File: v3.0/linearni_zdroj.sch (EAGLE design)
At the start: 29 parts, among them IC1 LM358N, IC2 LM358N, Q1 TIP120, Q2 TIP120

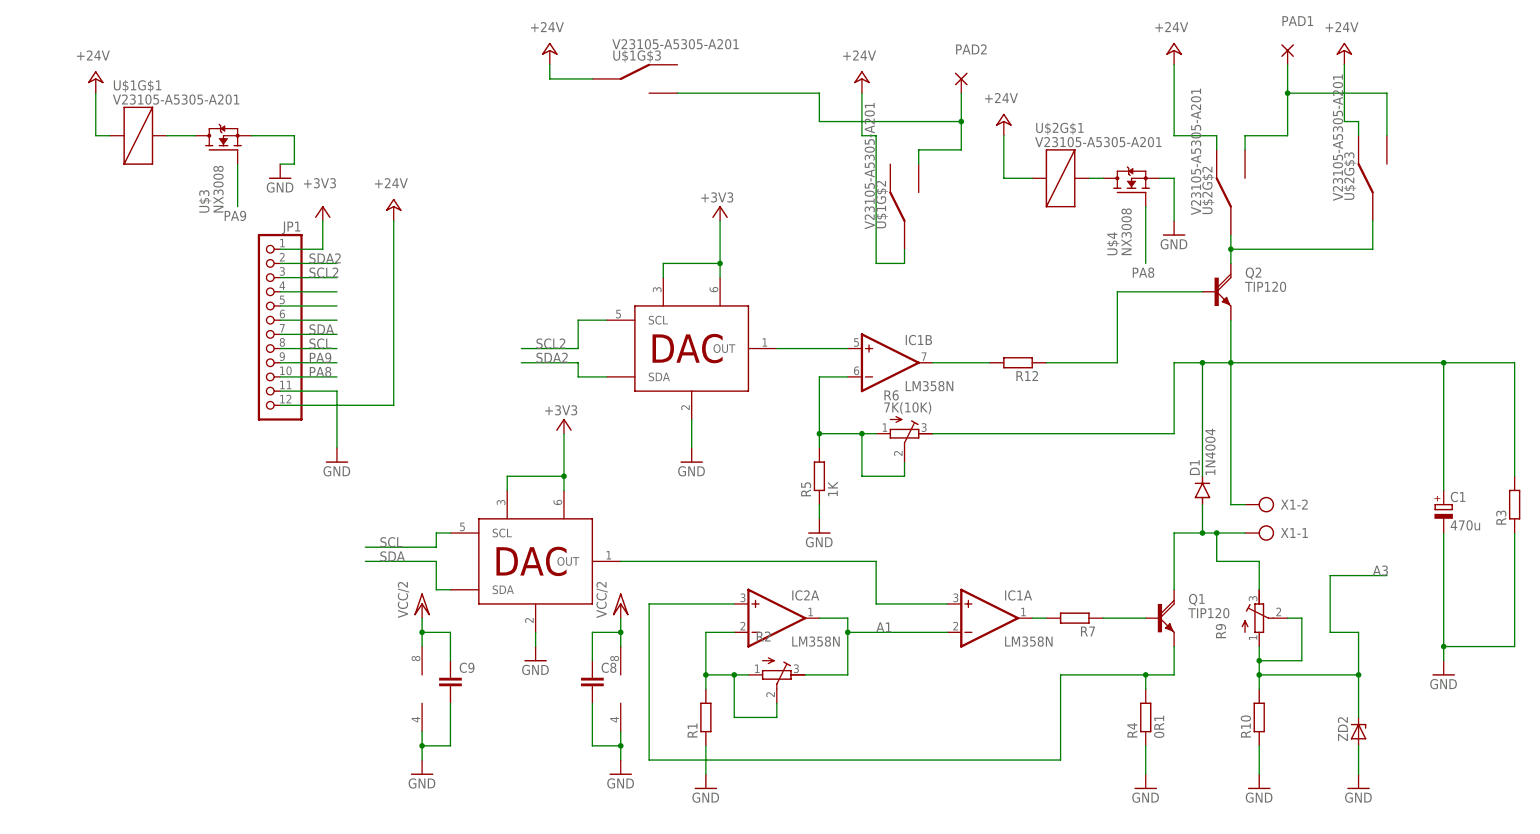
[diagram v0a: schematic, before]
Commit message: zpřehlednění schématu
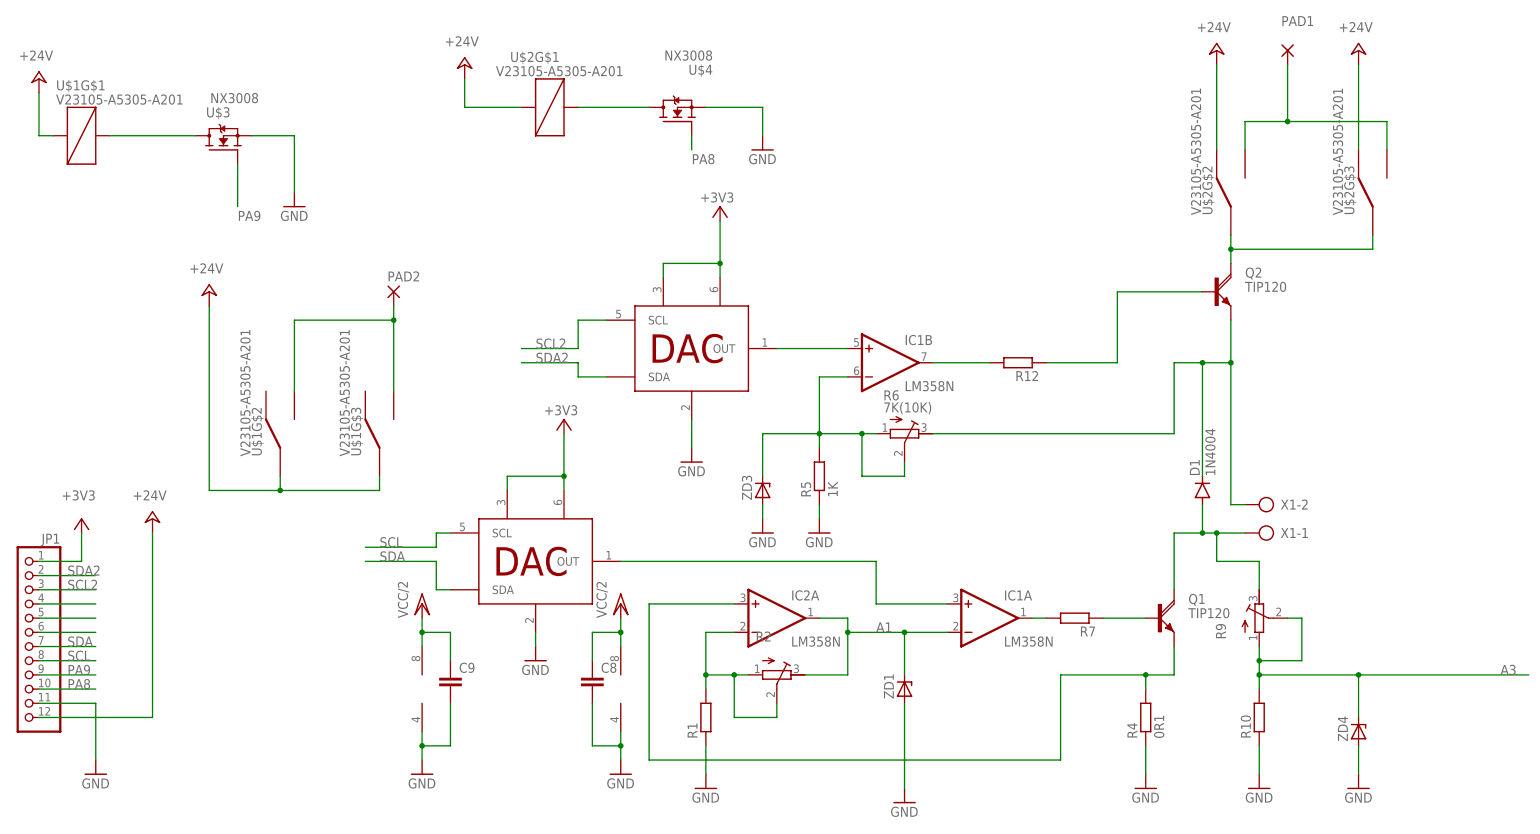
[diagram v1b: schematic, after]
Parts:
- removed C1: 470u, rcl:CPOL-EUE3.5-8
- removed R3: (no value), rcl:R-EU_R0805
- removed ZD2: (no value), devices:DIODE_ZENER5
- added ZD1, ZD3, ZD4: (no value), devices:DIODE_ZENER"2
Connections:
- net A1: now also ZD1.C
- net A3: now also ZD4.C; no longer ZD2.C
- net GND: now also ZD1.A, ZD3.A, ZD4.A; no longer C1.-, R3.1, ZD2.A
- net N$11: now also ZD3.C
- net N$13: no longer C1.+, R3.2
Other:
- moved on the sheet: JP1, PAD2, U$1G$1, U$1G$2, U$1G$3, U$2G$1, U$2G$3, U$4

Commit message: přidány pull-up rezistory I2C
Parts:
- added PAD3, PAD4: (no value), wirepad:3,81/1,4
- added R11, R13, R3, R8: (no value), rcl_my:R-EU_M0805
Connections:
- net +24V: now also PAD3.P, U$2G$2.3, U$2G$3.3; no longer U$2G$2.2, U$2G$3.2
- net +3V3: now also R11.2, R13.2, R3.2, R8.2
- net GND: now also PAD4.P
- net N$10: now also U$2G$2.2, U$2G$3.2; no longer U$2G$2.3, U$2G$3.3
- net SCL: now also R13.1
- net SCL2: now also R8.1
- net SDA: now also R3.1
- net SDA2: now also R11.1
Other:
- moved on the sheet: C9, PAD2, U$1G$2, U$1G$3

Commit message: deska lineárního regulátoru
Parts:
- removed C8: (no value), rcl:C-EUC0805
- added C1: (no value), rcl:C-EUC0805
- added R14: (no value), rcl:R-EU_R0805
- added ZD2: (no value), devices:DIODE_ZENER7
- D1: value 1N4004 -> (none); device diode:1N4004 -> devices:DIODE7
- Q1: value TIP120 -> IRFZ34NAV; device transistor-power:TIP120 -> devices:IRFZ34NAV
- R2, R6, R9: device rcl:R-TRIMM3339P -> pot:TRIM_EU-CA6V
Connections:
- removed net A1: IC1A.-IN, IC2A.OUT, R2.E, ZD1.C
- removed net A3: R10.2, R9.A, R9.S, ZD4.C
- removed net N$11: IC1B.-IN, R5.2, R6.A, R6.S, ZD3.C
- removed net N$14: JP1.4
- removed net N$15: JP1.5
- removed net N$18: JP1.6
- removed net VCC/2: C8.1, C9.1, IC1P.V+, IC2P.V+
- new net ADC0: IC2A.OUT, IC2B.-IN, JP1.6, R2.E, ZD1.C
- new net ADC1: JP1.5, R10.2, R9.A, R9.S, ZD4.C
- new net ADC2: IC1B.-IN, JP1.4, R5.2, R6.A, R6.S, ZD3.C
- new net N$20: C1.1, IC2A.+IN, R14.1
- net +24V: now also IC1P.V+, R7.2
- net GND: now also C1.2, ZD2.A; no longer C8.2
- net N$1: now also Q1.S, R14.2; no longer IC2A.+IN, Q1.E
- net N$2: now also IC2B.OUT, Q1.G; no longer IC1A.OUT, R7.2
- net N$5: now also C9.1, IC2P.V+, ZD2.C; no longer Q1.B
- net N$6: now also IC2B.+IN; no longer IC1A.+IN
- net N$7: now also Q1.D; no longer Q1.C
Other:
- moved on the sheet: R7

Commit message: přidání 3D modelu úpravy dokumentace
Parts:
- R1, R11, R13, R3, R8: device rcl_my:R-EU_M0805 -> rcl:R-EU_R0805

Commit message: upratování schémy, dokumentace lineárního regulátoru napětí
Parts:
- removed PAD1, PAD2: (no value), wirepad:3,81/1,4
- added C2: 10n, rcl:C-EUC0805
- added VSTUP-BUCK, VÝSTUP-BUCK: (no value), wirepad:3,81/1,4
- R11, R8: value (none) -> 5K
- R12: value (none) -> 360R
- renumbered PAD3 to 24V
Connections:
- net N$13 renamed +
- net N$8 renamed NAPAJENI-REG
- net +24V: now also C2.1
- net GND: now also C2.2
- net N$10: now also VÝSTUP-BUCK.P; no longer PAD1.P
- net N$19: now also VSTUP-BUCK.P; no longer PAD2.P
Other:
- note added: "Lineární regulátor napětí"
- note added: "Relé napájení pulzního regulátoru"
- note added: "Relé zdroje lineárních regulátorů"
- note added: "napájení OZ"
- moved on the sheet: IC1B, Q2, R11, R12, R13, R3, R5, R6, R8, U$1G$2, U$1G$3, U$2G$1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

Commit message: zase sem se jednou ve škole něco naučil
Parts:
- removed C1: (no value), rcl:C-EUC0805
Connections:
- removed net N$1: Q1.S, R14.2, R4.2
- net GND: now also R14.1; no longer C1.2
- net N$2: now also R14.2
- net N$20: now also Q1.S, R4.2; no longer C1.1, R14.1
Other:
- moved on the sheet: R14
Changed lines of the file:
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@@
 <part name="+3V6" library="supply1" library_urn="urn:adsk.eagle:library:371" deviceset="+3V3" device=""/>
 <part name="+3V7" library="supply1" library_urn="urn:adsk.eagle:library:371" deviceset="+3V3" device=""/>
-<part name="R14" library="rcl" library_urn="urn:adsk.eagle:library:334" deviceset="R-EU_" device="R0805" package3d_urn="urn:adsk.eagle:package:23553/2"/>
-<part name="C1" library="rcl" library_urn="urn:adsk.eagle:library:334" deviceset="C-EU" device="C0805" package3d_urn="urn:adsk.eagle:package:23617/2"/>
-<part name="GND8" library="supply1" library_urn="urn:adsk.eagle:library:371" deviceset="GND" device=""/>
 <part name="Q1" library="devices" deviceset="IRFZ34N" device="AV" override_package3d_urn="urn:adsk.eagle:package:33936961/2" override_package_urn="urn:adsk.eagle:footprint:33936962/1"/>
 <part name="P+5" library="supply1" library_urn="urn:adsk.eagle:library:371" deviceset="+24V" device=""/>
@@
 <part name="C2" library="rcl" library_urn="urn:adsk.eagle:library:334" deviceset="C-EU" device="C0805" package3d_urn="urn:adsk.eagle:package:23617/2" value="10n"/>
 <part name="+3V8" library="supply1" library_urn="urn:adsk.eagle:library:371" deviceset="+3V3" device=""/>
+<part name="GND8" library="supply1" library_urn="urn:adsk.eagle:library:371" deviceset="GND" device=""/>
+<part name="R14" library="rcl" library_urn="urn:adsk.eagle:library:334" deviceset="R-EU_" device="R0805" package3d_urn="urn:adsk.eagle:package:23553/2"/>
 </parts>
 <sheets>
@@
 <attribute name="VALUE" x="269.24" y="154.94" size="1.778" layer="96" rot="R180"/>
 </instance>
-<instance part="R14" gate="G$1" x="50.8" y="27.94" smashed="yes">
-<attribute name="NAME" x="46.99" y="29.4386" size="1.778" layer="95"/>
-<attribute name="VALUE" x="46.99" y="24.638" size="1.778" layer="96"/>
-</instance>
-<instance part="C1" gate="G$1" x="40.64" y="22.86" smashed="yes">
-<attribute name="NAME" x="42.164" y="23.241" size="1.778" layer="95"/>
-<attribute name="VALUE" x="42.164" y="18.161" size="1.778" layer="96"/>
-</instance>
-<instance part="GND8" gate="1" x="40.64" y="12.7" smashed="yes">
-<attribute name="VALUE" x="38.1" y="10.16" size="1.778" layer="96"/>
-</instance>
 <instance part="Q1" gate="G$1" x="109.22" y="55.88" smashed="yes">
 <attribute name="NAME" x="114.3" y="58.42" size="1.778" layer="95"/>
@@
 <instance part="+3V8" gate="G$1" x="287.02" y="149.86" smashed="yes">
 <attribute name="VALUE" x="289.56" y="152.4" size="1.778" layer="96" rot="R180"/>
+</instance>
+<instance part="GND8" gate="1" x="96.52" y="22.86" smashed="yes">
+<attribute name="VALUE" x="93.98" y="20.32" size="1.778" layer="96"/>
+</instance>
+<instance part="R14" gate="G$1" x="96.52" y="43.18" smashed="yes" rot="R90">
+<attribute name="NAME" x="95.0214" y="39.37" size="1.778" layer="95" rot="R90"/>
+<attribute name="VALUE" x="99.822" y="39.37" size="1.778" layer="96" rot="R90"/>
 </instance>
 </instances>
@@
 </busses>
 <nets>
-<net name="N$1" class="0">
-<segment>
-<wire x1="111.76" y1="43.18" x2="106.68" y2="43.18" width="0.1524" layer="91"/>
-<wire x1="106.68" y1="43.18" x2="91.44" y2="43.18" width="0.1524" layer="91"/>
-<wire x1="91.44" y1="43.18" x2="91.44" y2="27.94" width="0.1524" layer="91"/>
-<pinref part="R4" gate="G$1" pin="2"/>
-<wire x1="106.68" y1="40.64" x2="106.68" y2="43.18" width="0.1524" layer="91"/>
-<junction x="106.68" y="43.18"/>
-<wire x1="111.76" y1="50.8" x2="111.76" y2="43.18" width="0.1524" layer="91"/>
-<wire x1="91.44" y1="27.94" x2="55.88" y2="27.94" width="0.1524" layer="91"/>
-<pinref part="R14" gate="G$1" pin="2"/>
-<pinref part="Q1" gate="G$1" pin="S"/>
-</segment>
-</net>
 <net name="N$3" class="0">
 <segment>
@@
 <segment>
 <pinref part="GND8" gate="1" pin="GND"/>
-<pinref part="C1" gate="G$1" pin="2"/>
-<wire x1="40.64" y1="15.24" x2="40.64" y2="17.78" width="0.1524" layer="91"/>
+<wire x1="96.52" y1="25.4" x2="96.52" y2="38.1" width="0.1524" layer="91"/>
+<pinref part="R14" gate="G$1" pin="1"/>
 </segment>
 </net>
@@
 <wire x1="17.78" y1="55.88" x2="33.02" y2="55.88" width="0.1524" layer="91"/>
 <wire x1="17.78" y1="27.94" x2="17.78" y2="55.88" width="0.1524" layer="91"/>
-<wire x1="45.72" y1="27.94" x2="40.64" y2="27.94" width="0.1524" layer="91"/>
-<pinref part="R14" gate="G$1" pin="1"/>
-<pinref part="C1" gate="G$1" pin="1"/>
-<wire x1="40.64" y1="27.94" x2="17.78" y2="27.94" width="0.1524" layer="91"/>
-<wire x1="40.64" y1="25.4" x2="40.64" y2="27.94" width="0.1524" layer="91"/>
-<junction x="40.64" y="27.94"/>
+<wire x1="91.44" y1="27.94" x2="17.78" y2="27.94" width="0.1524" layer="91"/>
+<wire x1="111.76" y1="43.18" x2="106.68" y2="43.18" width="0.1524" layer="91"/>
+<wire x1="106.68" y1="43.18" x2="91.44" y2="43.18" width="0.1524" layer="91"/>
+<wire x1="91.44" y1="43.18" x2="91.44" y2="27.94" width="0.1524" layer="91"/>
+<pinref part="R4" gate="G$1" pin="2"/>
+<wire x1="106.68" y1="40.64" x2="106.68" y2="43.18" width="0.1524" layer="91"/>
+<junction x="106.68" y="43.18"/>
+<wire x1="111.76" y1="50.8" x2="111.76" y2="43.18" width="0.1524" layer="91"/>
+<pinref part="Q1" gate="G$1" pin="S"/>
 </segment>
 </net>
@@
 <pinref part="IC2" gate="B" pin="OUT"/>
 <pinref part="Q1" gate="G$1" pin="G"/>
-<wire x1="86.36" y1="53.34" x2="106.68" y2="53.34" width="0.1524" layer="91"/>
-</segment>
-</net>
+<wire x1="86.36" y1="53.34" x2="96.52" y2="53.34" width="0.1524" layer="91"/>
+<pinref part="R14" gate="G$1" pin="2"/>
+<wire x1="96.52" y1="53.34" x2="106.68" y2="53.34" width="0.1524" layer="91"/>
+<wire x1="96.52" y1="48.26" x2="96.52" y2="53.34" width="0.1524" layer="91"/>
+<junction x="96.52" y="53.34"/>
+</segment>
+</net>

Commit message: neumím malovat XD
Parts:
- removed ZD2: (no value), devices:DIODE_ZENER7
- Q2: value TIP120 -> (none); device transistor-power:TIP120 -> transistor:-NPN-TO220V
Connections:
- removed net N$5: C9.1, IC2P.V+, R7.1, ZD2.C
- new net N$1: IC2B.OUT, R7.2
- net +24V: now also C9.1, IC2P.V+; no longer R7.2
- net GND: no longer ZD2.A
- net N$2: now also R7.1; no longer IC2B.OUT
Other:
- moved on the sheet: R14, R7

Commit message: pokračování v doku úklid schéma
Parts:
- removed PAD4: (no value), wirepad:3,81/1,4
- removed R4: 0R1, rcl:R-EU_0411/15
- removed U$1, U$2: V23105-A5305-A201, realatka:V23105-A5305-A201
- removed U$3, U$4: NX3008, NEXPERIA :NX3008
- removed X1: (no value), con-ptr500:AK500/2
- added -: (no value), con-ptr500:AK500/2
- added ER1, ER2: V23105-A5305, realatka:V23105-A5305-A201
- added GND: (no value), wirepad:3,81/1,4
- added Q3, Q4: 2N7002, NEXPERIA :NX3008
- added RS: 0R1, rcl:R-EU_0411/15
- C9: value (none) -> 10n
- D1: value (none) -> 1N4001
- Q2: value (none) -> TIP120
- R1, R10: value (none) -> 1K
- R13, R3: value (none) -> 5K
- R14: value (none) -> 100K
- R2: value (none) -> 10K(9K)
- R7: value (none) -> 20K
- R9: value (none) -> 10K(7K)
- ZD1, ZD3, ZD4: value (none) -> 3,3V
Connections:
- net +: now also --2.KL; no longer X1-2.KL
- net +24V: now also ER1G$1.C$1, ER1G$2.1, ER1G$3.1, ER2G$1.C$1, ER2G$2.3, ER2G$3.3; no longer U$1G$1.C$1, U$1G$2.1, U$1G$3.1, U$2G$1.C$1, U$2G$2.3, U$2G$3.3
- net GND: now also GND.P, Q3.S, Q4.S, RS.1; no longer PAD4.P, R4.1, U$3.S, U$4.S
- net N$10: now also ER2G$2.2, ER2G$3.2; no longer U$2G$2.2, U$2G$3.2
- net N$16: now also ER1G$1.C$2, Q3.D; no longer U$1G$1.C$2, U$3.D
- net N$17: now also ER2G$1.C$2, Q4.D; no longer U$2G$1.C$2, U$4.D
- net N$19: now also ER1G$2.3, ER1G$3.3; no longer U$1G$2.3, U$1G$3.3
- net N$20: now also RS.2; no longer R4.2
- net N$7: now also --1.KL; no longer X1-1.KL
- net NAPAJENI-REG: now also ER2G$2.1, ER2G$3.1; no longer U$2G$2.1, U$2G$3.1
- net PA8: now also Q4.G; no longer U$4.G
- net PA9: now also Q3.G; no longer U$3.G
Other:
- note added: "Deska lineárních regulátorů"
- note added: "Lineární regulátor proudu"
- note added: "konektor řízení"
- note added: "ovládání cívek relé"
- moved on the sheet: 24V, C2, C9, D1, IC1B, IC2A, IC2B, JP1, Q1, Q2, R1, R10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
